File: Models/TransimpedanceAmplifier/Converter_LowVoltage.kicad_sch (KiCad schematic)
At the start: 0 parts

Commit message: Added the 3.3V regulator choice
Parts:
- added C9: 1 uF, symbol Device:C
- added D10: D_Schottky, symbol Device:D_Schottky
- added U8: TLV76133, 3.3V, 1%, DCY0004A-IPC_A, symbol TLV761:PTLV76118DCYR
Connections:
- new net: D10.1 (K), U8.3 (IN)
- new net: C9.1, D10.2 (A), U8.4 (OUT)
- new net GND: C9.2, U8.1 (GND)
- no-connect marks 0 -> 1

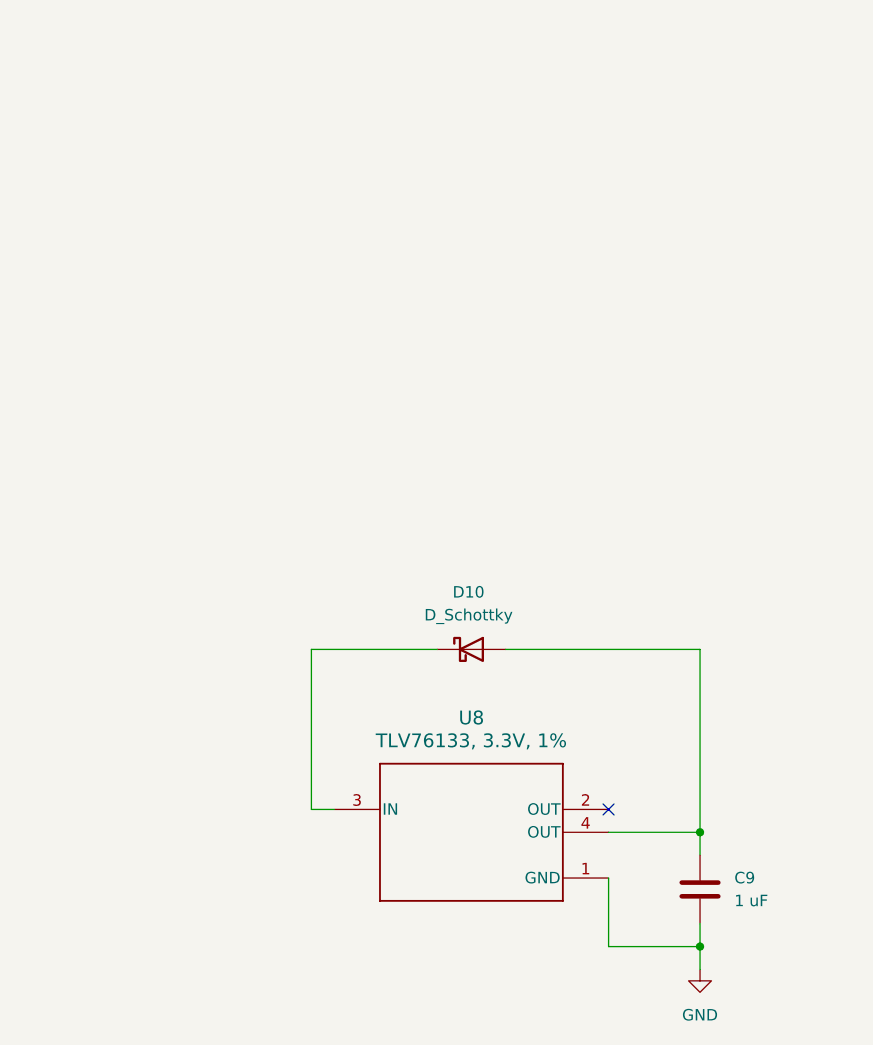
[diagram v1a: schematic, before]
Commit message: Labeled all the input/output nodes of the power subsystems
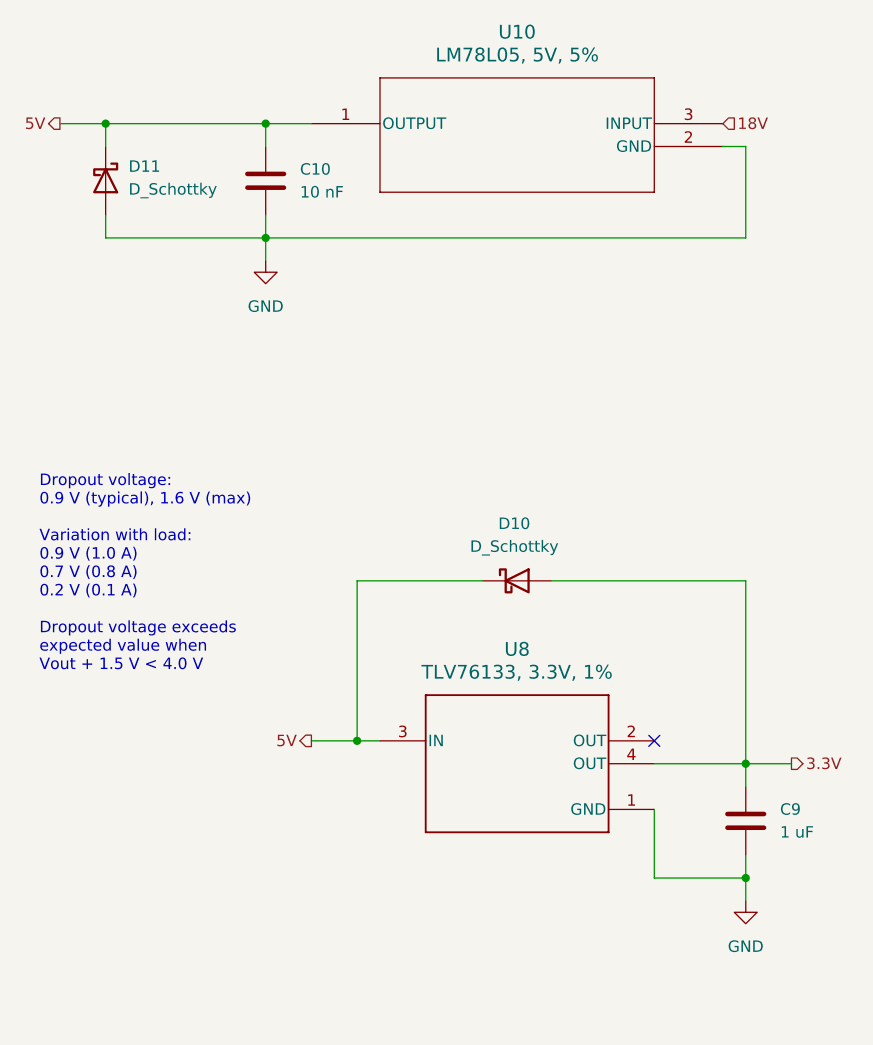
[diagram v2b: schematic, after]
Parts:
- added C10: 10 nF, symbol Device:C
- added D11: D_Schottky, symbol Device:D_Schottky
- added U10: LM78L05, 5V, 5%, LP3_TEX, symbol LM78L:LM78L05ACZ_LFT1
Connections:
- net GND: now also C10.2, D11.2 (A), U10.2 (GND)
- net 5V: now reaches D10.1 (K), U8.3 (IN)
- net 5V: now also C10.1, D11.1 (K), U10.1 (OUTPUT)
- net 3.3V: now reaches C9.1, D10.2 (A), U8.4 (OUT)
- new net 18V: U10.3 (INPUT)
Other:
- note added: "Dropout voltage: 0.9 V (typical), 1.6 V (max) Variation with load: 0.9 V (1.0 A) 0.7 V (0.8 A) 0.2 V (0.1 A) Dropout voltage exceeds expected value when Vout + 1.5 V < 4.0 V"
- moved on the sheet: C9, D10, U8
